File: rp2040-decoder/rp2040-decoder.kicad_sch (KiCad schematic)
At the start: 57 parts, among them J4 5052702412, Q1 TPM2008, Q2 TPM2008, Q3 TPM2008, Q4 TPM2008, Q5 TPM2008, Q6 TPM2008, Q7 TPM2008, U1 W25Q64JVXGIQ, U2 AP63203WU, U3 RP2040, U4 MD9927, U5 MAX98357A, U6 LMV331, Y1 X252012MMB4SI

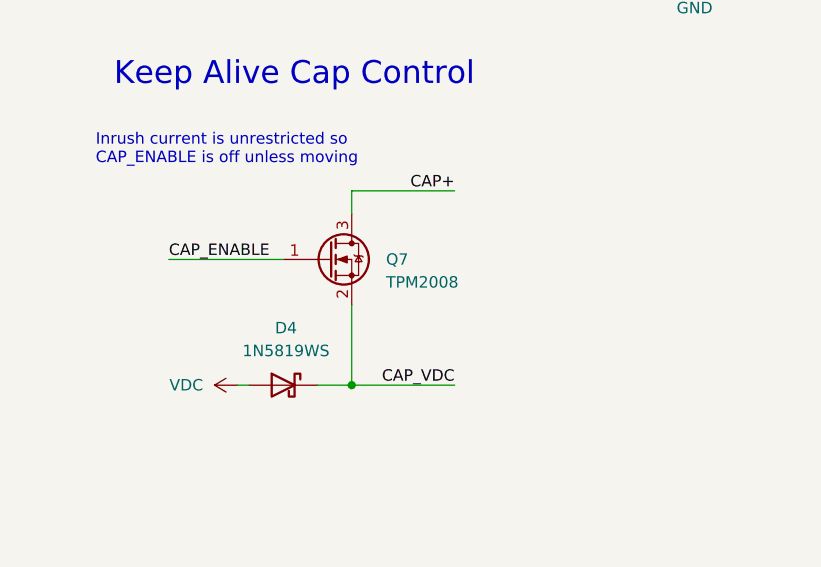
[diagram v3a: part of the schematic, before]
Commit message: fix: allow cap to discharge below 8V rail voltage
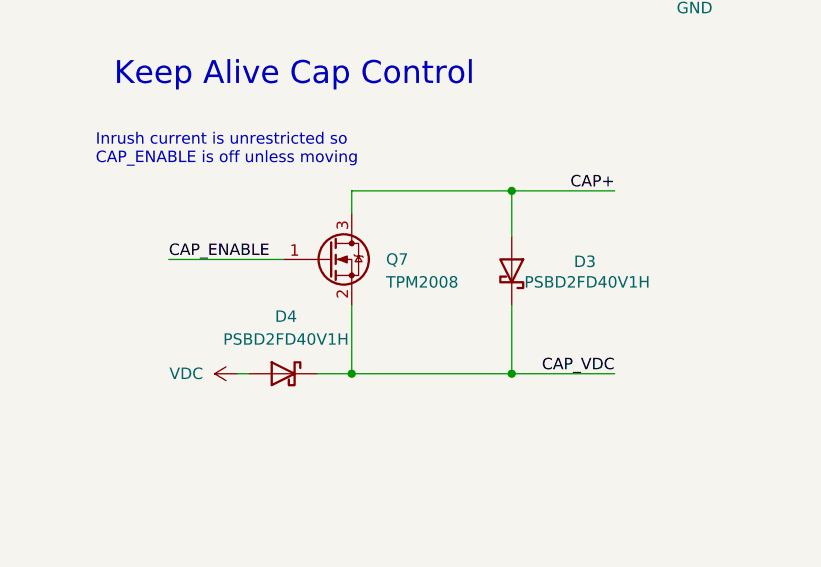
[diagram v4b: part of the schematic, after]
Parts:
- added D3: PSBD2FD40V1H, Diode_SMD:D_SOD-882, symbol Device:D_Schottky
- D4: value 1N5819WS -> PSBD2FD40V1H; footprint Diode_SMD:D_SOD-323 -> Diode_SMD:D_SOD-882; LCSC C191023 -> C492733
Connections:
- net CAP+: now also D3.2 (A)
- net CAP_VDC: now also D3.1 (K)
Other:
- moved on the sheet: D4
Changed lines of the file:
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@@
 	)
 	(junction
+		(at 138.43 85.09)
+		(diameter 0)
+		(color 0 0 0 0)
+	)
+	(junction
 		(at 256.54 161.29)
 		(diameter 0)
@@
 	)
 	(junction
+		(at 138.43 105.41)
+		(diameter 0)
+		(color 0 0 0 0)
+	)
+	(junction
 		(at 46.99 102.87)
 		(diameter 0)
@@
 	)
 	(junction
-		(at 120.65 106.68)
-		(diameter 0)
-		(color 0 0 0 0)
-	)
-	(junction
 		(at 218.44 143.51)
 		(diameter 0)
@@
 		(color 0 0 0 0)
 	)
+	(junction
+		(at 120.65 105.41)
+		(diameter 0)
+		(color 0 0 0 0)
+	)
 	(no_connect
 		(at 237.49 207.01)
@@
 	(wire
 		(pts
+			(xy 138.43 85.09) (xy 149.86 85.09)
+		)
+		(stroke
+			(width 0)
+			(type default)
+		)
+	)
+	(wire
+		(pts
 			(xy 233.68 82.55) (xy 233.68 83.82)
 		)
@@
 	(wire
 		(pts
+			(xy 120.65 105.41) (xy 120.65 97.79)
+		)
+		(stroke
+			(width 0)
+			(type default)
+		)
+	)
+	(wire
+		(pts
 			(xy 104.14 153.67) (xy 111.76 153.67)
 		)
@@
 	(wire
 		(pts
-			(xy 116.84 106.68) (xy 120.65 106.68)
+			(xy 116.84 105.41) (xy 120.65 105.41)
 		)
 		(stroke
@@
 	(wire
 		(pts
-			(xy 120.65 106.68) (xy 132.08 106.68)
+			(xy 120.65 105.41) (xy 138.43 105.41)
 		)
 		(stroke
@@
 	(wire
 		(pts
-			(xy 132.08 85.09) (xy 120.65 85.09)
+			(xy 120.65 85.09) (xy 138.43 85.09)
 		)
 		(stroke
@@
 	(wire
 		(pts
+			(xy 138.43 105.41) (xy 149.86 105.41)
+		)
+		(stroke
+			(width 0)
+			(type default)
+		)
+	)
+	(wire
+		(pts
 			(xy 212.09 163.83) (xy 212.09 162.56)
 		)
@@
 	(wire
 		(pts
-			(xy 120.65 106.68) (xy 120.65 97.79)
-		)
-		(stroke
-			(width 0)
-			(type default)
-		)
-	)
-	(wire
-		(pts
 			(xy 234.95 204.47) (xy 237.49 204.47)
 		)
@@
 	(wire
 		(pts
+			(xy 138.43 90.17) (xy 138.43 85.09)
+		)
+		(stroke
+			(width 0)
+			(type default)
+		)
+	)
+	(wire
+		(pts
 			(xy 172.72 179.07) (xy 184.15 179.07)
 		)
@@
 	(wire
 		(pts
-			(xy 107.95 106.68) (xy 109.22 106.68)
+			(xy 107.95 105.41) (xy 109.22 105.41)
 		)
 		(stroke
@@
 	(wire
 		(pts
+			(xy 138.43 97.79) (xy 138.43 105.41)
+		)
+		(stroke
+			(width 0)
+			(type default)
+		)
+	)
+	(wire
+		(pts
 			(xy 341.63 153.67) (xy 326.39 153.67)
 		)
@@
 	)
 	(label "CAP_VDC"
-		(at 132.08 106.68 180)
+		(at 149.86 105.41 180)
 		(effects
 			(font
@@
 	)
 	(label "CAP+"
-		(at 132.08 85.09 180)
+		(at 149.86 85.09 180)
 		(effects
 			(font
@@
 	(symbol
 		(lib_id "Device:D_Schottky")
-		(at 113.03 106.68 0)
+		(at 113.03 105.41 0)
 		(mirror y)
 		(unit 1)
@@
 		(dnp no)
 		(property "Reference" "D4"
-			(at 113.3475 100.33 0)
+			(at 113.3475 99.06 0)
 			(effects
 				(font
@@
 			)
 		)
-		(property "Value" "1N5819WS"
-			(at 113.3475 102.87 0)
+		(property "Value" "PSBD2FD40V1H"
+			(at 113.3475 101.6 0)
 			(effects
 				(font
@@
 			)
 		)
-		(property "Footprint" "Diode_SMD:D_SOD-323"
-			(at 113.03 106.68 0)
+		(property "Footprint" "Diode_SMD:D_SOD-882"
+			(at 113.03 105.41 0)
 			(effects
 				(font
@@
 			)
 		)
-		(property "Datasheet" "https://www.lcsc.com/datasheet/lcsc_datasheet_2409300937_Guangdong-Hottech-1N5819WS_C191023.pdf"
-			(at 113.03 106.68 0)
+		(property "Datasheet" "https://www.lcsc.com/datasheet/lcsc_datasheet_2003091236_Shanghai-Prisemi-Elec-PSBD2FD40V1H_C492733.pdf"
+			(at 113.03 105.41 0)
 			(effects
 				(font
@@
 		)
 		(property "Description" "Schottky diode"
-			(at 113.03 106.68 0)
+			(at 113.03 105.41 0)
 			(effects
 				(font
@@
 			)
 		)
-		(property "LCSC" "C191023"
-			(at 113.03 106.68 0)
+		(property "LCSC" "C492733"
+			(at 113.03 105.41 0)
 			(effects
 				(font
@@
 	(symbol
 		(lib_id "power:VDC")
-		(at 107.95 106.68 90)
+		(at 107.95 105.41 90)
 		(unit 1)
 		(exclude_from_sim no)
@@
 		(fields_autoplaced yes)
 		(property "Reference" "#PWR039"
-			(at 111.76 106.68 0)
+			(at 111.76 105.41 0)
 			(effects
 				(font
@@
 		)
 		(property "Value" "VDC"
-			(at 104.14 106.6799 90)
+			(at 104.14 105.4099 90)
 			(effects
 				(font
@@
 		)
 		(property "Footprint" ""
-			(at 107.95 106.68 0)
+			(at 107.95 105.41 0)
 			(effects
 				(font
@@
 		)
 		(property "Datasheet" ""
-			(at 107.95 106.68 0)
+			(at 107.95 105.41 0)
 			(effects
 				(font
@@
 		)
 		(property "Description" "Power symbol creates a global label with name \"VDC\""
-			(at 107.95 106.68 0)
+			(at 107.95 105.41 0)
 			(effects
 				(font
@@
 					(unit 1)
 				)
+			)
+		)
+	)
+	(symbol
+		(lib_id "Device:D_Schottky")
+		(at 138.43 93.98 270)
+		(mirror x)
+		(unit 1)
+		(exclude_from_sim no)
+		(in_bom yes)
+		(on_board yes)
+		(dnp no)
+		(property "Reference" "D3"
+			(at 146.558 92.964 90)
+			(effects
+				(font
+					(size 1.27 1.27)
+				)
+			)
+		)
+		(property "Value" "PSBD2FD40V1H"
+			(at 146.812 95.25 90)
+			(effects
+				(font
+					(size 1.27 1.27)
+				)
+			)
+		)
+		(property "Footprint" "Diode_SMD:D_SOD-882"
+			(at 138.43 93.98 0)
+			(effects
+				(font
+					(size 1.27 1.27)
+				)
+				(hide yes)
+			)
+		)
+		(property "Datasheet" "https://www.lcsc.com/datasheet/lcsc_datasheet_2003091236_Shanghai-Prisemi-Elec-PSBD2FD40V1H_C492733.pdf"
+			(at 138.43 93.98 0)
+			(effects
+				(font
+					(size 1.27 1.27)
+				)
+				(hide yes)
+			)
+		)
+		(property "Description" "Schottky diode"
+			(at 138.43 93.98 0)
+			(effects
+				(font
+					(size 1.27 1.27)
+				)
+				(hide yes)
+			)
+		)
+		(property "LCSC" "C492733"
+			(at 138.43 93.98 0)
+			(effects
+				(font
+					(size 1.27 1.27)
+				)
+				(hide yes)
+			)
+		)
+		(pin "1"
+		)
+		(pin "2"
+		)
+		(instances
+			(project "rp2040-decoder"
+				(path "/139be664-fb54-41f1-a01f-7316e3835554"
+					(reference "D3")
+					(unit 1)
+				)

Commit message: chore: update schematic comments
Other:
- note added: "Ext. Capacitor Charge Control"
- note added: "Ext. Capacitor Low Rail Voltage Cutoff"
- note added: "Inrush current is restricted only by PWMing CAP_ENABLE. 100% duty cycle not recommended with large caps, and only after receiving move command"
- note removed: "Inrush current is unrestricted so CAP_ENABLE is off unless moving"
- note removed: "Keep Alive Cap Control"
- note removed: "Keep Alive Cap Low Voltage Cutoff"
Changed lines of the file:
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@@
 		)
 	)
-	(text "Inrush current is unrestricted so \nCAP_ENABLE is off unless moving"
+	(text "Inrush current is restricted only by PWMing CAP_ENABLE. 100% duty cycle\nnot recommended with large caps, and only after receiving move command"
 		(exclude_from_sim no)
-		(at 92.202 82.296 0)
+		(at 92.202 80.518 0)
 		(effects
 			(font
@@
 		)
 	)
-	(text "Keep Alive Cap Low Voltage Cutoff"
+	(text "Ext. Capacitor Low Rail Voltage Cutoff"
 		(exclude_from_sim no)
-		(at 17.526 73.406 0)
+		(at 14.732 73.406 0)
 		(effects
 			(font
@@
 		)
 	)
-	(text "Keep Alive Cap Control"
+	(text "Ext. Capacitor Charge Control"
 		(exclude_from_sim no)
 		(at 94.234 73.66 0)

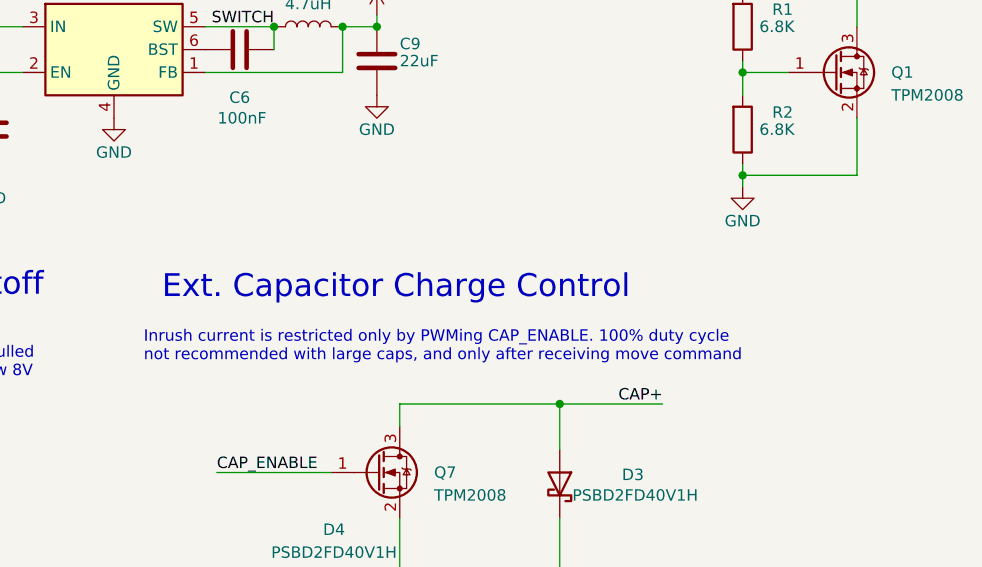
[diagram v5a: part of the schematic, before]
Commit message: fix: update footprints and component rotations
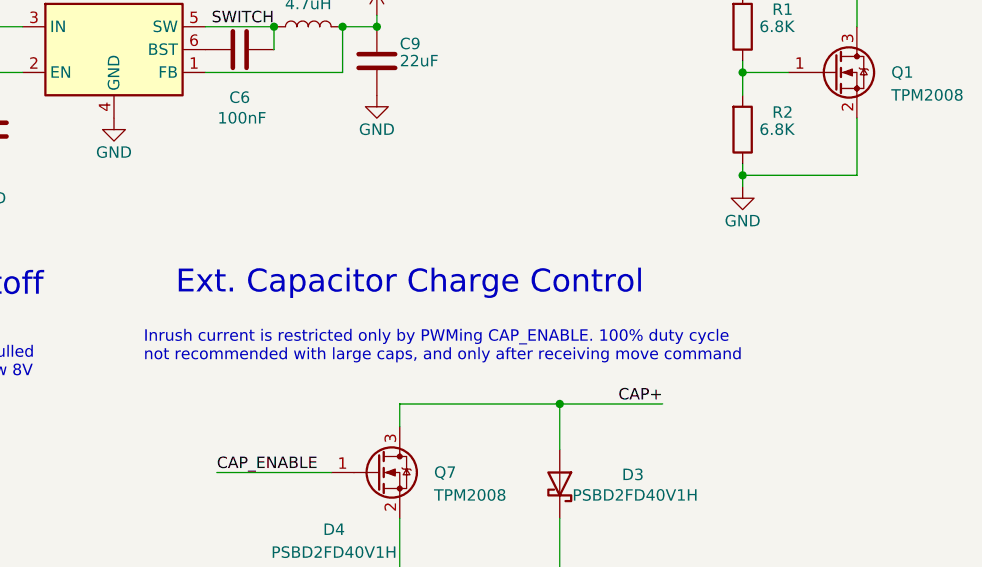
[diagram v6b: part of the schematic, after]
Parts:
- D1: JLCPCB_CORRECTION -0.25;0;0 -> 0;-0.25;0
- Q2: JLCPCB_CORRECTION 0;0;90 -> 0;0;-90
- Q5: JLCPCB_CORRECTION 0;0;-90 -> 0;0;90
- U1: footprint Local Library:W25Q64JVXGIQ -> Package_SON:WSON-8-1EP_4x4mm_P0.8mm_EP2.2x3mm; JLCPCB_CORRECTION 0;0;90 -> 0;0;0
- U2: JLCPCB_CORRECTION (none) -> 0;0;-90
- U6: JLCPCB_CORRECTION (none) -> 0;0;180
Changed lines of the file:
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@@
 	(text "Ext. Capacitor Charge Control"
 		(exclude_from_sim no)
-		(at 94.234 73.66 0)
+		(at 95.758 73.152 0)
 		(effects
 			(font
@@
 			)
 		)
+		(property "JLCPCB_CORRECTION" "0;0;-90"
+			(at 88.9 45.72 0)
+			(effects
+				(font
+					(size 1.27 1.27)
+				)
+				(hide yes)
+			)
+		)
 		(pin "6"
 		)
@@
 			)
 		)
-		(property "JLCPCB_CORRECTION" "0;0;90"
+		(property "JLCPCB_CORRECTION" "0;0;-90"
 			(at 337.82 46.99 0)
 			(effects
@@
 			)
 		)
-		(property "Datasheet" ""
+		(property "Datasheet" "https://www.lcsc.com/datasheet/lcsc_datasheet_2101111937_Shanghai-Mingda-Microelectronics-MD9927_C2684662.pdf"
 			(at 355.6 213.36 0)
 			(effects
@@
 			)
 		)
-		(property "JLCPCB_CORRECTION" "-0.25;0;0"
+		(property "JLCPCB_CORRECTION" "0;-0.25;0"
 			(at 49.53 48.26 0)
 			(effects
@@
 			)
 		)
-		(property "Footprint" "Local Library:W25Q64JVXGIQ"
+		(property "Footprint" "Package_SON:WSON-8-1EP_4x4mm_P0.8mm_EP2.2x3mm"
 			(at 120.65 176.53 0)
 			(effects
@@
 			)
 		)
-		(property "Description" "64Mb Serial Flash Memory, Standard/Dual/Quad SPI, WSON-8"
+		(property "Description" "64Mb Serial Flash Memory, Standard/Dual/Quad SPI, XSON-8"
 			(at 120.65 171.45 0)
 			(effects
@@
 			)
 		)
-		(property "JLCPCB_CORRECTION" "0;0;90"
+		(property "JLCPCB_CORRECTION" "0;0;0"
 			(at 120.65 199.39 0)
 			(effects
@@
 			)
 		)
+		(property "JLCPCB_CORRECTION" "0;0;180"
+			(at 49.53 95.25 0)
+			(effects
+				(font
+					(size 1.27 1.27)
+				)
+				(hide yes)
+			)
+		)
 		(pin "3"
 		)
@@
 			)
 		)
-		(property "JLCPCB_CORRECTION" "0;0;-90"
+		(property "JLCPCB_CORRECTION" "0;0;90"
 			(at 367.03 46.99 0)
 			(effects

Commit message: fix: more dfm fixes
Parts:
- U1: footprint Package_SON:WSON-8-1EP_4x4mm_P0.8mm_EP2.2x3mm -> Package_DFN_QFN:DFN-8-1EP_4x4mm_P0.8mm_EP2.3x3.24mm
- U4: footprint Package_DFN_QFN:DFN-8-1EP_2x2mm_P0.5mm_EP0.9x1.6mm -> Local Library:LM293QT
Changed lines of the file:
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@@
 			)
 		)
-		(property "Footprint" "Package_DFN_QFN:DFN-8-1EP_2x2mm_P0.5mm_EP0.9x1.6mm"
+		(property "Footprint" "Local Library:LM293QT"
 			(at 355.6 213.36 0)
 			(effects
@@
 			)
 		)
-		(property "Footprint" "Package_SON:WSON-8-1EP_4x4mm_P0.8mm_EP2.2x3mm"
+		(property "Footprint" "Package_DFN_QFN:DFN-8-1EP_4x4mm_P0.8mm_EP2.3x3.24mm"
 			(at 120.65 176.53 0)
 			(effects

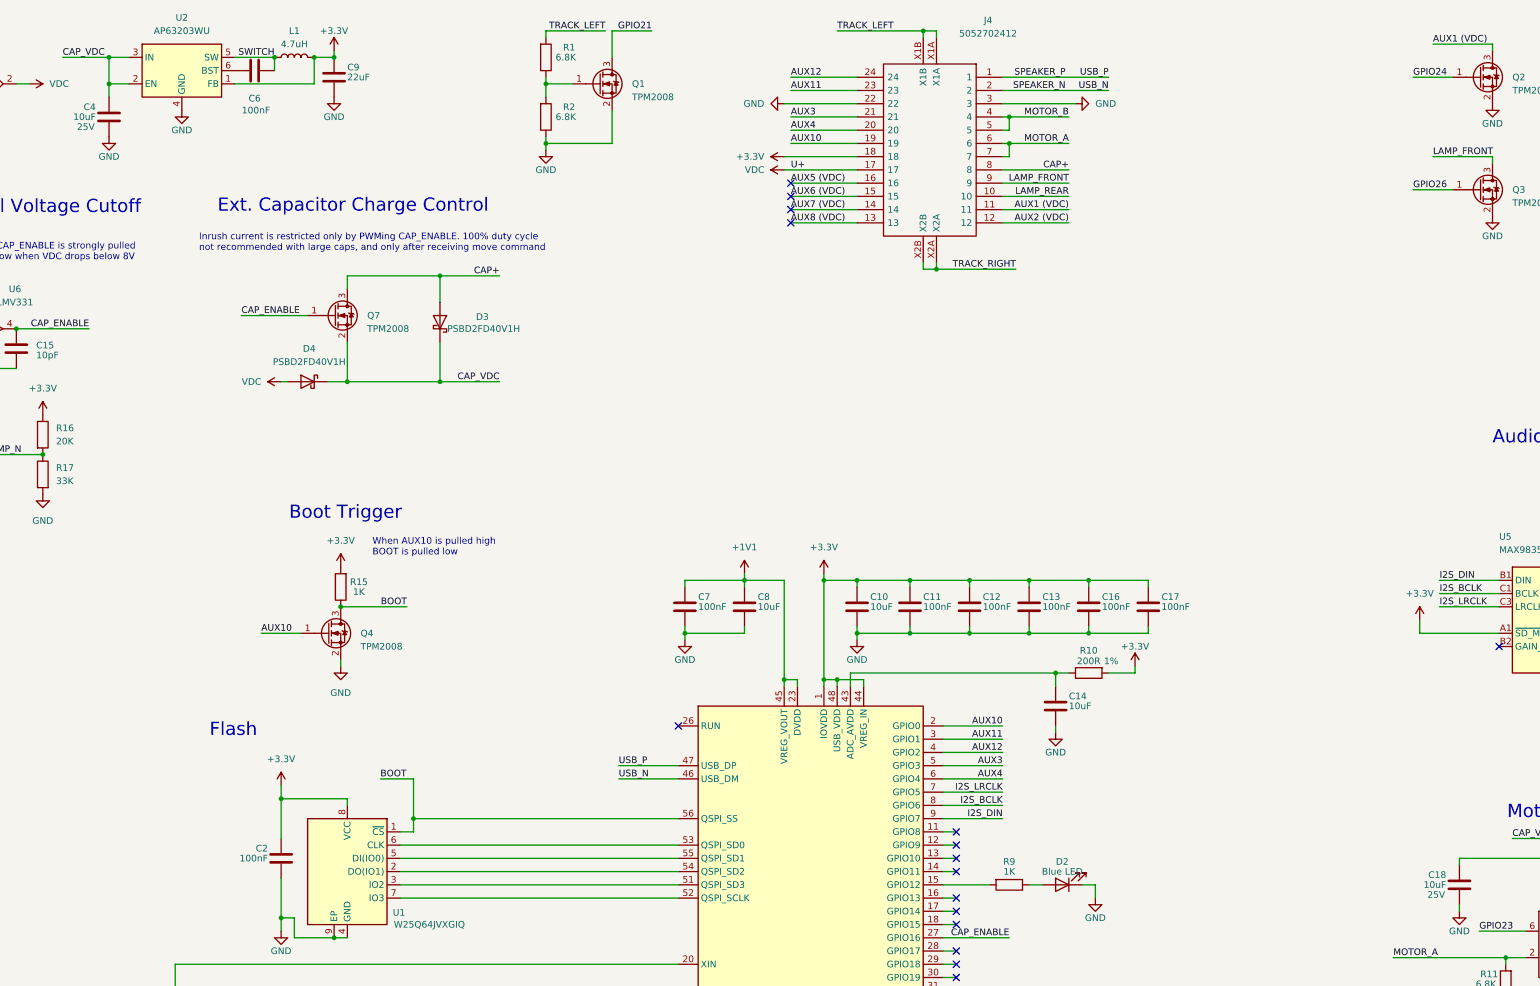
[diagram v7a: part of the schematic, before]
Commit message: feat: increase motor driver cap to 47uF
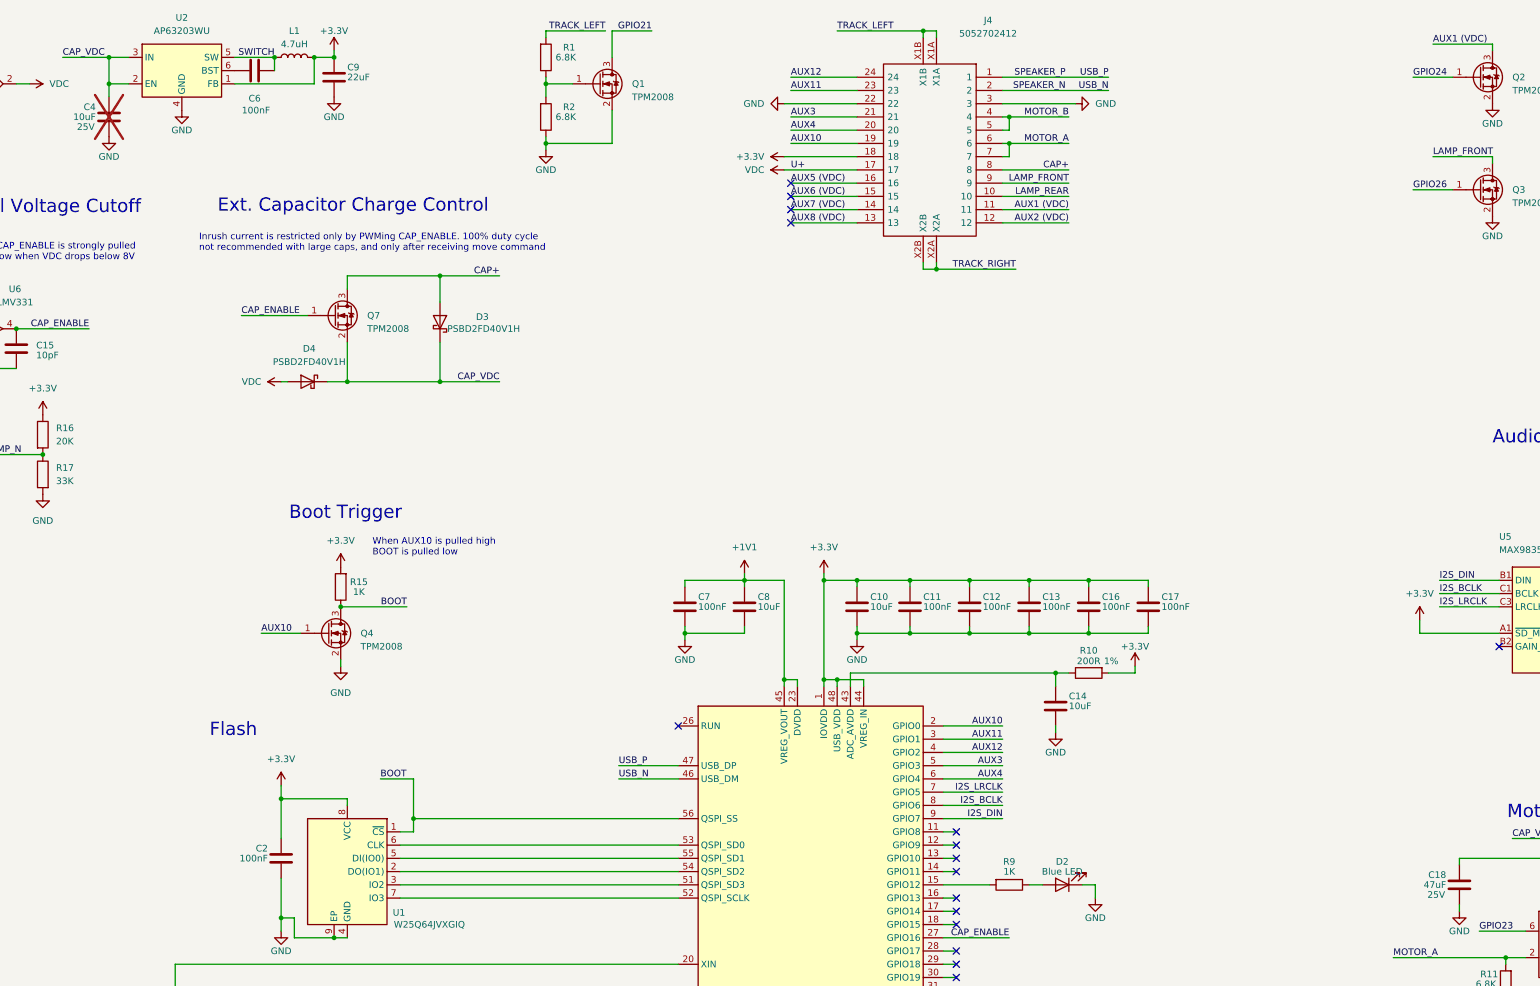
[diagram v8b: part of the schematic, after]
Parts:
- C18: value 10uF -> 47uF; footprint Capacitor_SMD:C_0603_1608Metric -> Capacitor_SMD:C_1206_3216Metric; LCSC C96446 -> C403725
- C4: now not fitted; now left out of the parts list
- U1: footprint Package_DFN_QFN:DFN-8-1EP_4x4mm_P0.8mm_EP2.3x3.24mm -> Package_SON:WSON-8-1EP_4x4mm_P0.8mm_EP2.2x3mm
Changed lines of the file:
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@@
 			)
 		)
-		(property "Value" "10uF"
+		(property "Value" "47uF"
 			(at 331.47 201.93 0)
 			(effects
@@
 			)
 		)
-		(property "Footprint" "Capacitor_SMD:C_0603_1608Metric"
+		(property "Footprint" "Capacitor_SMD:C_1206_3216Metric"
 			(at 333.0448 205.74 0)
 			(effects
@@
 			)
 		)
-		(property "LCSC" "C96446"
+		(property "LCSC" "C403725"
 			(at 334.01 201.93 0)
 			(effects
@@
 			)
 		)
-		(property "Footprint" "Package_DFN_QFN:DFN-8-1EP_4x4mm_P0.8mm_EP2.3x3.24mm"
+		(property "Footprint" "Package_SON:WSON-8-1EP_4x4mm_P0.8mm_EP2.2x3mm"
 			(at 120.65 176.53 0)
 			(effects
@@
 		(unit 1)
 		(exclude_from_sim no)
-		(in_bom yes)
-		(on_board yes)
-		(dnp no)
+		(in_bom no)
+		(on_board no)
+		(dnp yes)
 		(property "Reference" "C4"
 			(at 72.39 52.705 0)
@@
 			)
 		)
-		(property "Description" ""
+		(property "Description" "Redundant to motor driver VDC cap"
 			(at 74.93 54.61 0)
 			(effects
